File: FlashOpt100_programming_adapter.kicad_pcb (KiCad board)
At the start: 2 copper layers, 17.8 x 35.6 mm, 3 parts, among them J1 29F256, J2 29F256

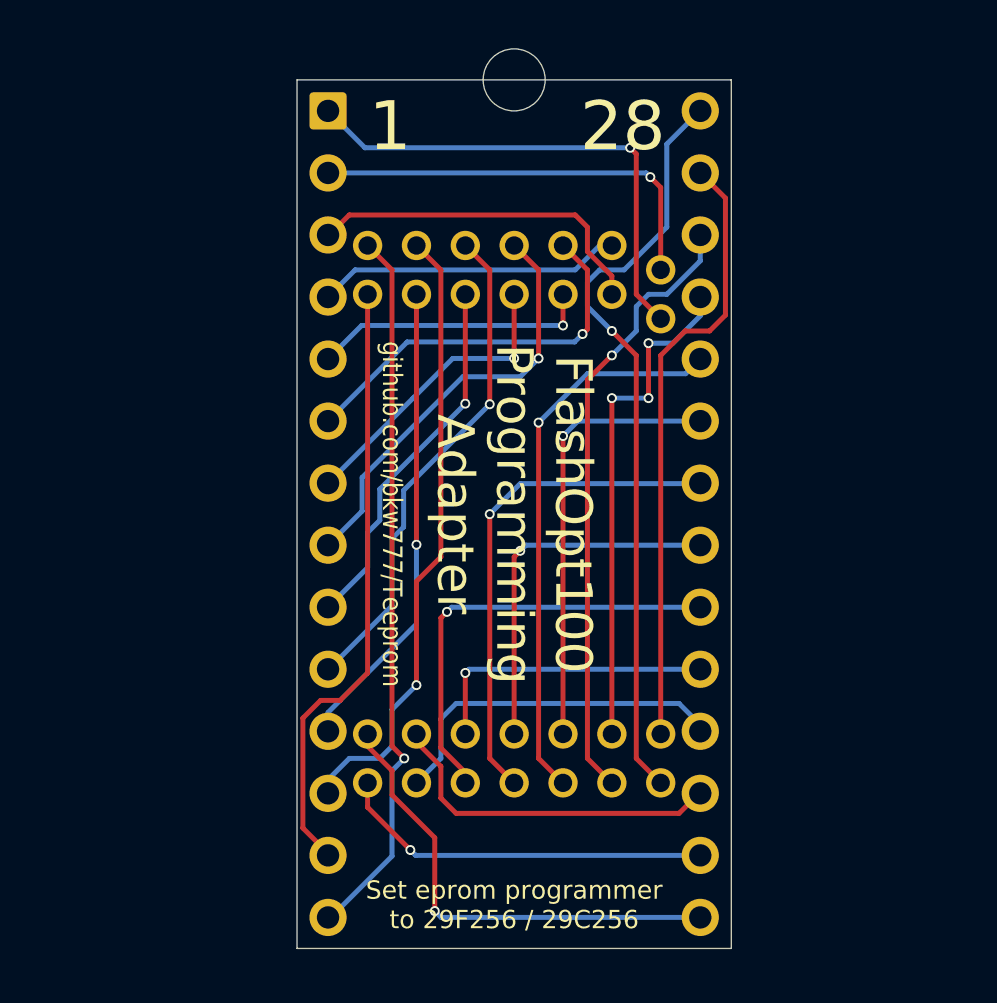
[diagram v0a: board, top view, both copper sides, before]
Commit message: flashopt100 prg routing & text
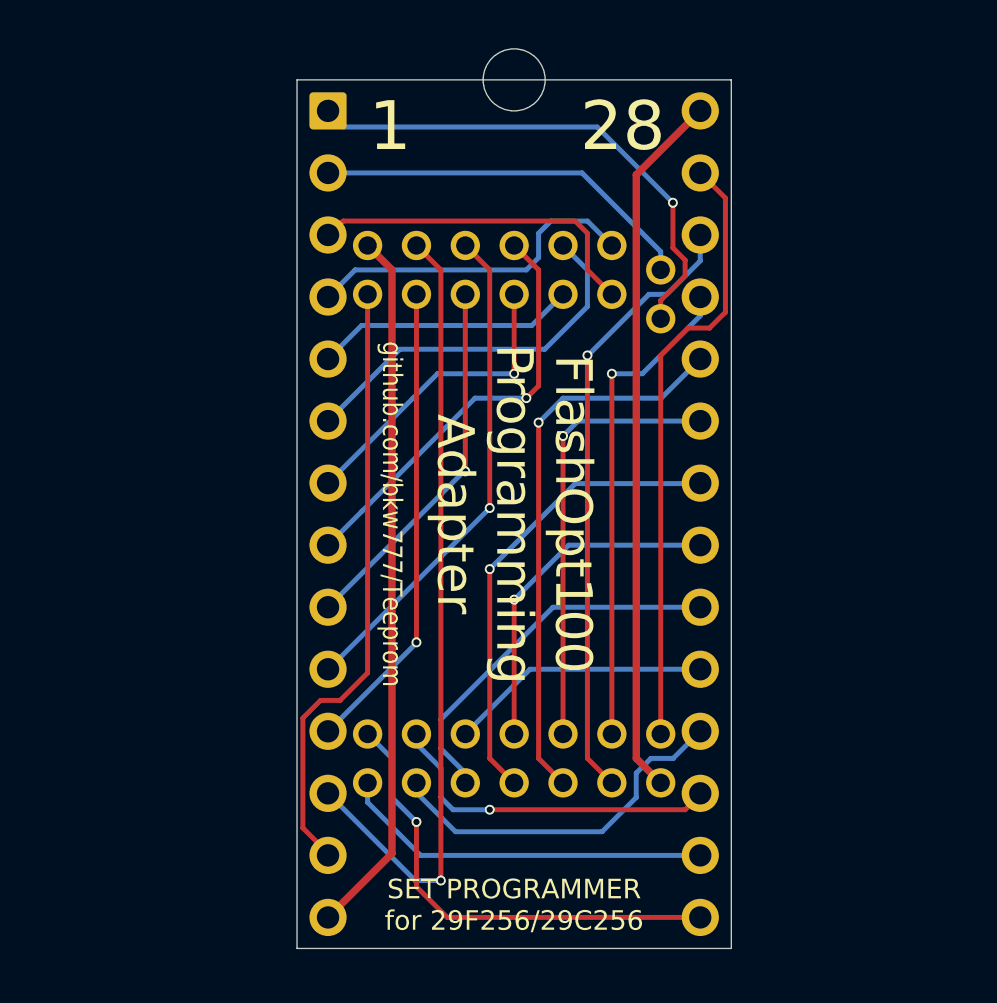
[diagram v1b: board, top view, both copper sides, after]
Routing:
- net /D1: track 25.5 -> 32.5 mm
- net /~CE: track 18.0 -> 15.5 mm, vias 1 -> 0
- net VCC: track 31.3 -> 29.0 mm, vias 1 -> 0
- net /A12: track 17.2 -> 15.7 mm, vias 1 -> 0
- net /D7: track 12.2 -> 10.7 mm, vias 1 -> 0
- net /A6: track 12.5 -> 13.9 mm
- net /~OE: track 20.6 -> 19.2 mm
- net /A10: track 15.1 -> 14.0 mm
- net /A5: track 11.5 -> 10.7 mm, vias 1 -> 0
- net /A8: track 20.9 -> 20.1 mm, vias 3 -> 1
- net /A4: track 16.0 -> 15.5 mm, vias 1 -> 0
- net /~WE: track 20.5 -> 21.0 mm
- net GND: track 29.5 -> 29.0 mm, vias 1 -> 0
- net /D4: track 15.4 -> 15.3 mm, vias 1 -> 0
- net /D5: track 14.3 -> 14.1 mm, vias 0 -> 1
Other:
- board text added: "CENTER PINS OTHER SIDE"
- board text added: "DIP28 PINS THIS SIDE"
- board text added: "SET PROGRAMMER for 29F256/29C256"
- board text removed: "Set eprom programmer to 29F256 / 29C256"

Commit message: completely new FlashOpt100 and programming adapter
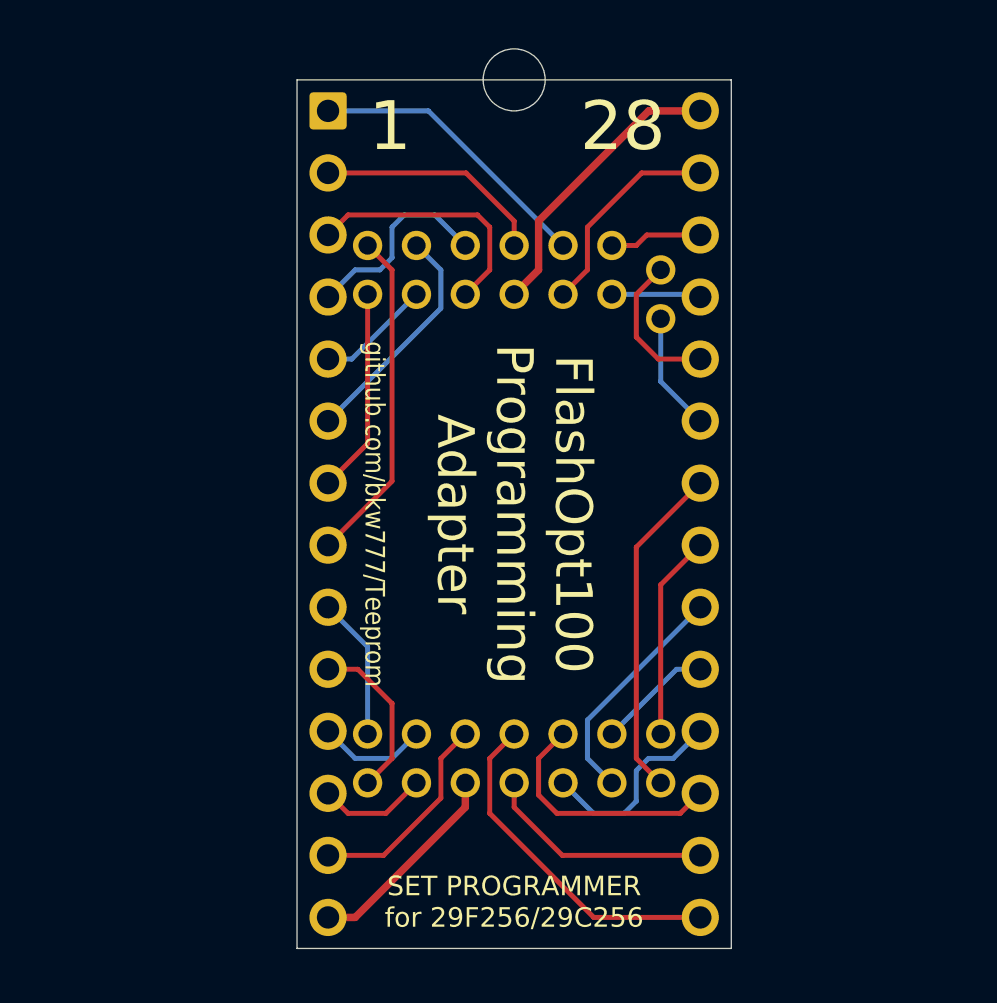
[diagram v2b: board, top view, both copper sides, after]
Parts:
- J1: value 29F256 -> 29F256 / 29C256
- J2: value 29F256 -> FlashOpt100_PRG_4x7; footprint 000_LOCAL:4x7_prg_2.0mm_male_straight -> 000_LOCAL:FlashOpt100_PRG_4x7_male
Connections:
- J2 pad 1: /~WE -> /A11
- J2 pad 10: /A0 -> /A6
- J2 pad 11: /D0 -> /A5
- J2 pad 12: /D1 -> /A4
- J2 pad 13: /D2 -> /A3
- J2 pad 14: GND -> /A2
- J2 pad 15: /D3 -> /A1
- J2 pad 16: /D4 -> /A0
- J2 pad 17: /D5 -> /D0
- J2 pad 18: /D6 -> /D1
- J2 pad 19: /D7 -> /D2
- J2 pad 2: /A12 -> /A9
- J2 pad 20: /~CE -> GND
- J2 pad 21: /A10 -> /D3
- J2 pad 22: /~OE -> /D4
- J2 pad 23: /A11 -> /D5
- J2 pad 24: /A9 -> /D6
- J2 pad 25: /A8 -> /D7
- J2 pad 26: /A13 -> /~CE
- J2 pad 27: /A14 -> /A10
- J2 pad 28: VCC -> /~OE
- J2 pad 3: /A7 -> /A8
- J2 pad 4: /A6 -> /A13
- J2 pad 5: /A5 -> /A14
- J2 pad 6: /A4 -> /~WE
- J2 pad 7: /A3 -> VCC
- J2 pad 8: /A2 -> /A12
- J2 pad 9: /A1 -> /A7
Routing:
- net /D1: track 32.5 -> 4.48 mm, vias 1 -> 0
- net /A13: track 25.2 -> 3.80 mm, vias 1 -> 0
- net GND: track 29.0 -> 8.49 mm
- net VCC: track 29.0 -> 11.9 mm
- net /A9: track 22.9 -> 6.16 mm, vias 1 -> 0
- net /A8: track 20.1 -> 3.67 mm, vias 1 -> 0
- net /D2: track 25.0 -> 8.63 mm
- net /A14: track 25.0 -> 8.70 mm
- net /D0: track 19.4 -> 4.49 mm, vias 1 -> 0
- net /A0: track 20.5 -> 6.86 mm, vias 1 -> 0
- net /A11: track 18.1 -> 4.86 mm, vias 1 -> 0
- net /A1: track 15.2 -> 5.86 mm, vias 1 -> 0
- net /~WE: track 21.0 -> 11.9 mm, vias 1 -> 0
- net /D6: track 15.2 -> 8.26 mm
- net /A12: track 15.7 -> 9.44 mm
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
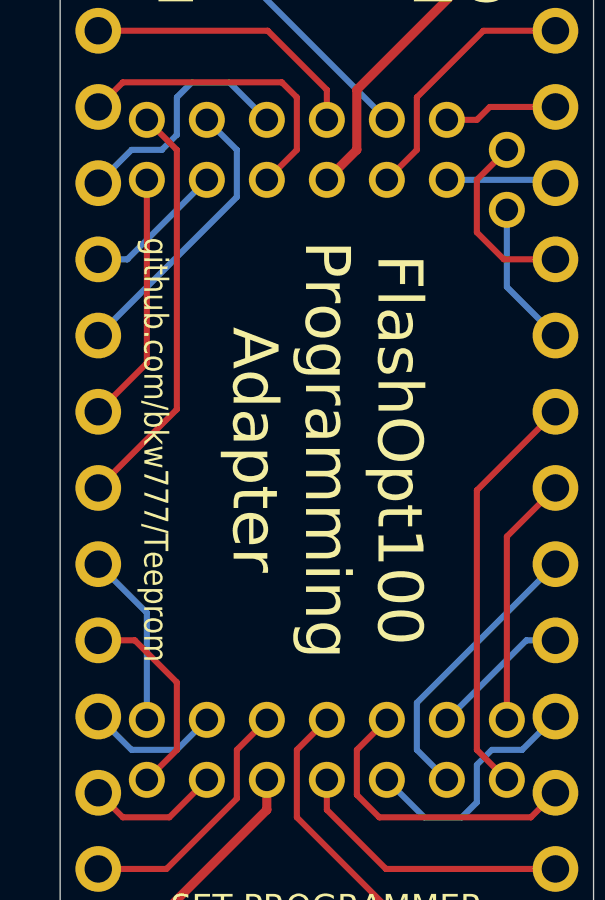
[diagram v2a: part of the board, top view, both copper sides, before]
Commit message: FlashOpt100 remove zone fill
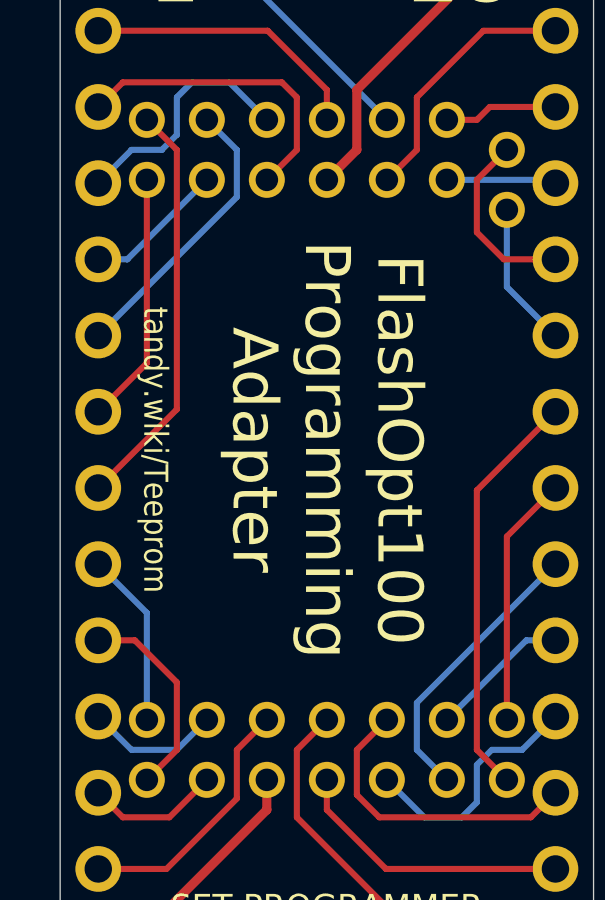
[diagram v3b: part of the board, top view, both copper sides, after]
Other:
- board text added: "tandy.wiki/Teeprom"
- board text removed: "github.com/bkw777/Teeprom"
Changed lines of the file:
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@@
   )
   (setup
-    (last_trace_width 0.3048)
+    (last_trace_width 0.1524)
     (user_trace_width 0.2032)
     (user_trace_width 0.25)
@@
     (effects (font (size 0.8 0.8) (thickness 0.12)))
   )
-  (gr_text github.com/bkw777/Teeprom (at 141.5034 99.187 -90) (layer F.SilkS)
+  (gr_text tandy.wiki/Teeprom (at 141.5034 99.187 -90) (layer F.SilkS)
     (effects (font (size 0.8 0.7) (thickness 0.1)))
   )

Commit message: silkscreen
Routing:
- net /D3: track 14.0 -> 11.8 mm
- net /A7: track 10.3 -> 8.33 mm
- net /D5: track 10.2 -> 8.33 mm
- net GND: track 8.49 -> 7.90 mm
- net /D4: track 9.44 -> 8.85 mm
- net /A12: track 9.44 -> 8.85 mm
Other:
- board text added: "DIP PINS THIS SIDE"
- board text added: "SET PROGRAMMER TO 29F256 / 29C256"
- board text removed: "DIP28 PINS THIS SIDE"
- board text removed: "SET PROGRAMMER for 29F256/29C256"
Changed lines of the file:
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@@
   (general
     (thickness 1.6)
-    (drawings 11)
-    (tracks 94)
+    (drawings 31)
+    (tracks 91)
     (zones 0)
     (modules 3)
@@
   )
   (setup
-    (last_trace_width 0.1524)
+    (last_trace_width 0.2032)
     (user_trace_width 0.2032)
     (user_trace_width 0.25)
@@
     (pad "" np_thru_hole circle (at 0 0) (size 2.54 2.54) (drill 2.54) (layers *.Cu *.Mask))
   )
-  (gr_text "DIP28 PINS\nTHIS SIDE" (at 147.2184 84.582) (layer B.SilkS)
+  (gr_line (start 154.2184 111.187) (end 140.2184 111.187) (layer F.SilkS) (width 0.1))
+  (gr_line (start 154.2184 107.187) (end 154.2184 111.187) (layer F.SilkS) (width 0.1))
+  (gr_line (start 140.2184 107.187) (end 154.2184 107.187) (layer F.SilkS) (width 0.1))
+  (gr_line (start 140.2184 111.187) (end 140.2184 107.187) (layer F.SilkS) (width 0.1))
+  (gr_line (start 152.2184 92.187) (end 152.2184 91.187) (layer F.SilkS) (width 0.1))
+  (gr_line (start 154.2184 92.187) (end 152.2184 92.187) (layer F.SilkS) (width 0.1))
+  (gr_line (start 154.2184 88.187) (end 154.2184 92.187) (layer F.SilkS) (width 0.1))
+  (gr_line (start 152.2184 88.187) (end 154.2184 88.187) (layer F.SilkS) (width 0.1))
+  (gr_line (start 152.2184 87.187) (end 140.2184 87.187) (layer F.SilkS) (width 0.1))
+  (gr_line (start 152.2184 91.187) (end 152.2184 87.187) (layer F.SilkS) (width 0.1))
+  (gr_line (start 140.2184 91.187) (end 152.2184 91.187) (layer F.SilkS) (width 0.1))
+  (gr_line (start 140.2184 87.187) (end 140.2184 91.187) (layer F.SilkS) (width 0.1))
+  (gr_line (start 153.6954 81.534) (end 155.9814 81.534) (layer B.SilkS) (width 0.1))
+  (gr_line (start 153.6954 116.84) (end 153.6954 81.534) (layer B.SilkS) (width 0.1))
+  (gr_line (start 155.9814 116.84) (end 153.6954 116.84) (layer B.SilkS) (width 0.1))
+  (gr_line (start 155.9814 81.534) (end 155.9814 116.84) (layer B.SilkS) (width 0.1))
+  (gr_line (start 140.7414 81.534) (end 138.4554 81.534) (layer B.SilkS) (width 0.1))
+  (gr_line (start 140.7414 116.84) (end 140.7414 81.534) (layer B.SilkS) (width 0.1))
+  (gr_line (start 138.4554 116.84) (end 140.7414 116.84) (layer B.SilkS) (width 0.1))
+  (gr_line (start 138.4554 81.534) (end 138.4554 116.84) (layer B.SilkS) (width 0.1))
+  (gr_text "DIP PINS\nTHIS SIDE" (at 147.2184 84.582) (layer B.SilkS)
     (effects (font (size 1 1) (thickness 0.1)) (justify mirror))
   )
@@
     (effects (font (size 1 1) (thickness 0.1)) (justify mirror))
   )
-  (gr_text "SET PROGRAMMER\nfor 29F256/29C256" (at 147.2184 115.062) (layer F.SilkS)
+  (gr_text "SET PROGRAMMER TO\n29F256 / 29C256" (at 147.2184 115.687) (layer F.SilkS)
     (effects (font (size 0.8 0.8) (thickness 0.12)))
   )
@@
   (gr_line (start 138.3284 81.407) (end 156.1084 81.407) (layer Edge.Cuts) (width 0.01))
   (gr_line (start 138.3284 116.967) (end 138.3284 81.407) (layer Edge.Cuts) (width 0.01))
-  (segment (start 150.4784 115.697) (end 154.8384 115.697) (width 0.2032) (layer Top) (net 1))
-  (segment (start 146.2184 111.437) (end 150.4784 115.697) (width 0.2032) (layer Top) (net 1))
-  (segment (start 146.2184 109.187) (end 146.2184 111.437) (width 0.2032) (layer Top) (net 1))
-  (segment (start 147.2184 108.187) (end 146.2184 109.187) (width 0.2032) (layer Top) (net 1))
+  (segment (start 148.2184 109.187) (end 147.2184 108.187) (width 0.2032) (layer Top) (net 1))
+  (segment (start 148.2184 110.937) (end 148.2184 109.187) (width 0.2032) (layer Top) (net 1))
+  (segment (start 152.9784 115.697) (end 148.2184 110.937) (width 0.2032) (layer Top) (net 1))
+  (segment (start 154.8384 115.697) (end 152.9784 115.697) (width 0.2032) (layer Top) (net 1))
   (segment (start 153.2184 102.077) (end 154.8384 100.457) (width 0.2032) (layer Top) (net 2))
   (segment (start 153.2184 108.187) (end 153.2184 102.077) (width 0.2032) (layer Top) (net 2))
-  (segment (start 147.2184 111.187) (end 147.2184 110.187) (width 0.2032) (layer Top) (net 3))
-  (segment (start 149.1884 113.157) (end 147.2184 111.187) (width 0.2032) (layer Top) (net 3))
-  (segment (start 154.8384 113.157) (end 149.1884 113.157) (width 0.2032) (layer Top) (net 3))
-  (segment (start 146.2184 89.187) (end 145.2184 90.187) (width 0.2032) (layer Top) (net 4))
-  (segment (start 146.2184 87.437) (end 146.2184 89.187) (width 0.2032) (layer Top) (net 4))
-  (segment (start 140.4184 86.937) (end 145.7184 86.937) (width 0.2032) (layer Top) (net 4))
-  (segment (start 145.7184 86.937) (end 146.2184 87.437) (width 0.2032) (layer Top) (net 4))
+  (segment (start 150.1884 113.157) (end 147.2184 110.187) (width 0.2032) (layer Bottom) (net 3))
+  (segment (start 154.8384 113.157) (end 150.1884 113.157) (width 0.2032) (layer Bottom) (net 3))
+  (segment (start 144.2184 89.187) (end 145.2184 90.187) (width 0.2032) (layer Top) (net 4))
+  (segment (start 144.2184 87.437) (end 144.2184 89.187) (width 0.2032) (layer Top) (net 4))
+  (segment (start 143.7184 86.937) (end 144.2184 87.437) (width 0.2032) (layer Top) (net 4))
+  (segment (start 140.4184 86.937) (end 143.7184 86.937) (width 0.2032) (layer Top) (net 4))
   (segment (start 139.5984 87.757) (end 140.4184 86.937) (width 0.2032) (layer Top) (net 4))
   (segment (start 154.0184 111.437) (end 154.8384 110.617) (width 0.2032) (layer Top) (net 5))
-  (segment (start 148.9684 111.437) (end 154.0184 111.437) (width 0.2032) (layer Top) (net 5))
-  (segment (start 148.2184 110.687) (end 148.9684 111.437) (width 0.2032) (layer Top) (net 5))
-  (segment (start 148.2184 109.187) (end 148.2184 110.687) (width 0.2032) (layer Top) (net 5))
-  (segment (start 149.2184 108.187) (end 148.2184 109.187) (width 0.2032) (layer Top) (net 5))
+  (segment (start 150.7184 111.437) (end 154.0184 111.437) (width 0.2032) (layer Top) (net 5))
+  (segment (start 150.2184 110.937) (end 150.7184 111.437) (width 0.2032) (layer Top) (net 5))
+  (segment (start 150.2184 109.187) (end 150.2184 110.937) (width 0.2032) (layer Top) (net 5))
+  (segment (start 149.2184 108.187) (end 150.2184 109.187) (width 0.2032) (layer Top) (net 5))
   (segment (start 143.9684 86.937) (end 145.2184 88.187) (width 0.2032) (layer Bottom) (net 6))
   (segment (start 142.7184 86.937) (end 143.9684 86.937) (width 0.2032) (layer Bottom) (net 6))
@@
   (segment (start 142.2184 109.187) (end 142.2184 106.937) (width 0.2032) (layer Top) (net 17))
   (segment (start 141.2184 110.187) (end 142.2184 109.187) (width 0.2032) (layer Top) (net 17))
-  (segment (start 147.2184 87.187) (end 147.2184 88.187) (width 0.2032) (layer Top) (net 18))
-  (segment (start 145.2484 85.217) (end 147.2184 87.187) (width 0.2032) (layer Top) (net 18))
-  (segment (start 139.5984 85.217) (end 145.2484 85.217) (width 0.2032) (layer Top) (net 18))
+  (segment (start 144.2484 85.217) (end 147.2184 88.187) (width 0.2032) (layer Top) (net 18))
+  (segment (start 139.5984 85.217) (end 144.2484 85.217) (width 0.2032) (layer Top) (net 18))
   (segment (start 140.7084 109.187) (end 139.5984 108.077) (width 0.2032) (layer Bottom) (net 19))
   (segment (start 142.2184 109.187) (end 140.7084 109.187) (width 0.2032) (layer Bottom) (net 19))
@@
   (segment (start 154.7284 90.187) (end 154.8384 90.297) (width 0.2032) (layer Bottom) (net 22))
   (segment (start 151.2184 90.187) (end 154.7284 90.187) (width 0.2032) (layer Bottom) (net 22))
-  (segment (start 144.2184 109.187) (end 145.2184 108.187) (width 0.2032) (layer Top) (net 23))
-  (segment (start 144.2184 110.812) (end 144.2184 109.187) (width 0.2032) (layer Top) (net 23))
-  (segment (start 141.8734 113.157) (end 144.2184 110.812) (width 0.2032) (layer Top) (net 23))
-  (segment (start 139.5984 113.157) (end 141.8734 113.157) (width 0.2032) (layer Top) (net 23))
+  (segment (start 144.2184 109.187) (end 145.2184 108.187) (width 0.2032) (layer Bottom) (net 23))
+  (segment (start 144.2184 110.937) (end 144.2184 109.187) (width 0.2032) (layer Bottom) (net 23))
+  (segment (start 141.9984 113.157) (end 144.2184 110.937) (width 0.2032) (layer Bottom) (net 23))
+  (segment (start 139.5984 113.157) (end 141.9984 113.157) (width 0.2032) (layer Bottom) (net 23))
   (segment (start 150.2184 109.187) (end 151.2184 110.187) (width 0.2032) (layer Bottom) (net 24))
   (segment (start 150.2184 107.617) (end 150.2184 109.187) (width 0.2032) (layer Bottom) (net 24))
@@
   (segment (start 148.2184 89.187) (end 148.2184 87.187) (width 0.3048) (layer Top) (net 27))
   (segment (start 147.2184 90.187) (end 148.2184 89.187) (width 0.3048) (layer Top) (net 27))
-  (segment (start 145.2184 111.187) (end 145.2184 110.187) (width 0.3048) (layer Top) (net 28))
-  (segment (start 140.7084 115.697) (end 145.2184 111.187) (width 0.3048) (layer Top) (net 28))
-  (segment (start 139.5984 115.697) (end 140.7084 115.697) (width 0.3048) (layer Top) (net 28))
+  (segment (start 139.7084 115.697) (end 145.2184 110.187) (width 0.3048) (layer Top) (net 28))
+  (segment (start 139.5984 115.697) (end 139.7084 115.697) (width 0.3048) (layer Top) (net 28))
 )
